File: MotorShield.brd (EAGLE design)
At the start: 85 x 56 mm, 119 parts, among them IC1 OPA4340E, IC2 OPA4340E, IC3 74HCT125D, X1 MSTBV2, X2 MSTBV8, X3 MSTBV8, X4 INPUTS, X5 BUTTON_LED, X6 DOTSTARS

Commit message: exchanged MCP3008 symbol and footprint https://github.com/hpbock/PCB-Designs/blob/master/!Libraries/MCP3008.lbr
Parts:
- removed U$58: MCP3008SO16, MSC3008:SO16
- added U$1: MCP3008SL, MCP3008:SO16
- C9: value 0,1uF -> 100nF; device eagle-ltspice:C0805 -> rcl:C0805
- moved X6 26.7 mm to (47.0, 29.8)
- moved X5 24.1 mm to (45.1, 44.5)
- moved C9 5.55 mm to (24.8, 41.9), flipped to the top
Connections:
- removed net 3,3V: C9.1, IC1.4, IC2.4, PCB1.1, PCB1.17, U$58.15, U$58.16
- new net +3,3V: IC1.4, IC2.4, PCB1.1, PCB1.17
- new net +3V3: C9.1, U$1.15, U$1.16
- net CH0: now also U$1.1; no longer U$58.1
- net CH1: now also U$1.2; no longer U$58.2
- net CH2: now also U$1.3; no longer U$58.3
- net CH3: now also U$1.4; no longer U$58.4
- net CH4: now also U$1.5; no longer U$58.5
- net CH5: now also U$1.6; no longer U$58.6
- net CH6: now also U$1.7; no longer U$58.7
- net CH7: now also U$1.8; no longer U$58.8
- net CLK: now also U$1.13; no longer U$58.13
- net CS_ADC: now also U$1.10; no longer U$58.10
- net DIN: now also U$1.11; no longer U$58.11
- net DOUT: now also U$1.12; no longer U$58.12
- net GND: now also U$1.14, U$1.9; no longer U$58.14, U$58.9
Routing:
- net +3V3: track 0.00 -> 6.10 mm, vias 0 -> 1

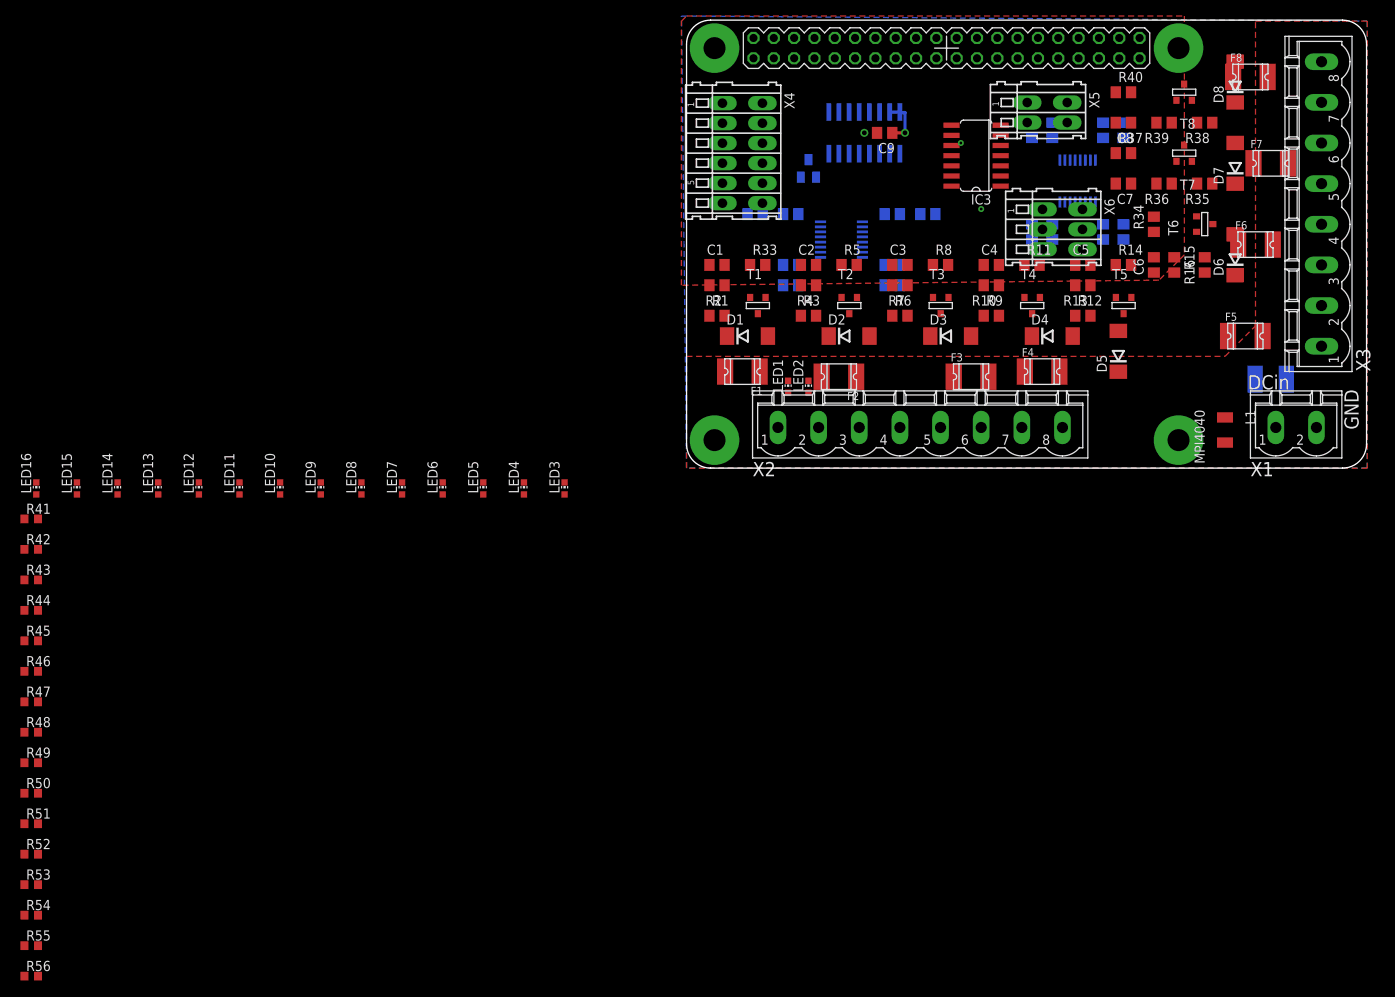
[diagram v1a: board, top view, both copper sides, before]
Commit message: added net classes and tried to place components for M1
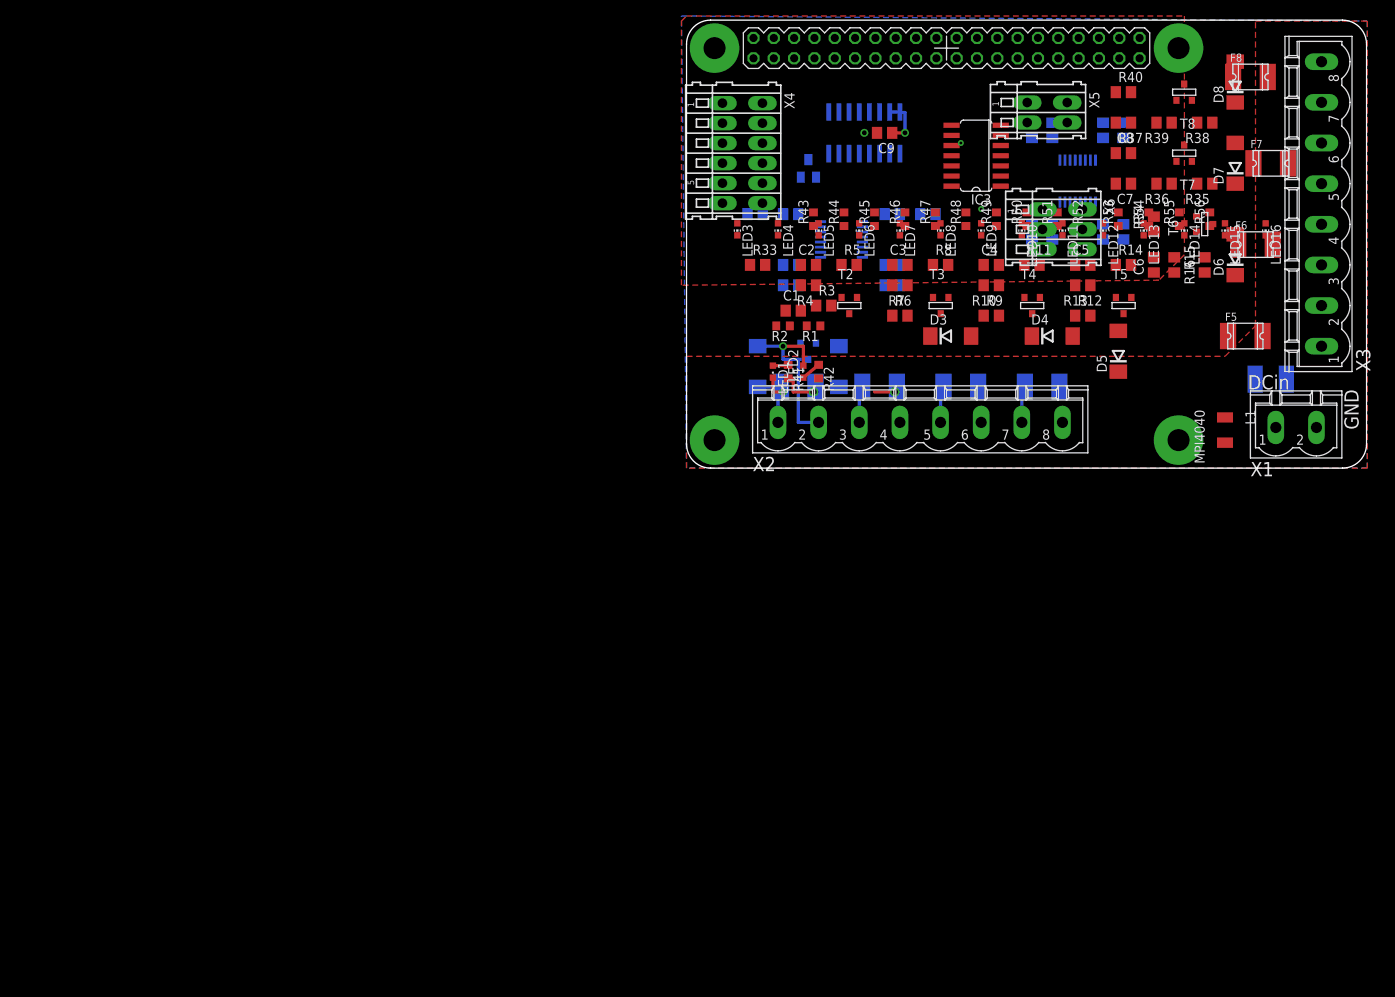
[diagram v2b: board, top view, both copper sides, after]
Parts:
- removed F1: 1812L, ptc-littlefuse:1812L
- added VIAMO: 1812L, ptc-littlefuse:1812L
- LED1, LED2: device led:CHIP-LED0603 -> led:CHIPLED_0603
- R1, R2: device rcl:R0805 -> rcl:R0603
- moved R56 175.1 mm to (65.4, 31.1), turned to 90 degrees
- moved R55 169.8 mm to (61.6, 31.1), turned to 90 degrees
- moved R54 164.6 mm to (57.8, 31.1), turned to 90 degrees
- moved R53 159.3 mm to (54.0, 31.1), turned to 90 degrees
- moved LED16 157.0 mm to (72.4, 29.8), turned to 180 degrees
- moved R52 154.1 mm to (50.2, 31.1), turned to 90 degrees
- moved R51 148.9 mm to (46.4, 31.1), turned to 90 degrees
- moved LED15 147.1 mm to (67.3, 29.8), turned to 180 degrees
- moved R50 143.7 mm to (42.5, 31.1), turned to 90 degrees
- moved R49 138.5 mm to (38.7, 31.1), turned to 90 degrees
- moved LED14 137.2 mm to (62.2, 29.8), turned to 180 degrees
- moved R48 133.3 mm to (34.9, 31.1), turned to 90 degrees
- moved R47 128.1 mm to (31.1, 31.1), turned to 90 degrees
- moved LED13 127.4 mm to (57.1, 29.8), turned to 180 degrees
- moved R46 123.0 mm to (27.3, 31.1), turned to 90 degrees
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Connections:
- removed net 5V: PCB1.2, PCB1.4
- net +24V: now also VIAMO.2; no longer F1.2
- net +3,3V: no longer PCB1.1
- net +3V3: now also PCB1.1
- net 24V/1A: now also VIAMO.1; no longer F1.1
- net VCC: now also PCB1.2, PCB1.4
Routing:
- net N$2: track 0.00 -> 23.4 mm, vias 0 -> 1
- net 24V/1A: track 0.00 -> 11.0 mm, vias 0 -> 1
- net +24V: track 0.00 -> 9.18 mm, vias 0 -> 2
- net N$9: track 0.00 -> 4.83 mm
- net N$12: track 0.00 -> 4.83 mm
- net N$13: track 0.00 -> 4.82 mm
- net N$30: track 0.00 -> 2.59 mm
- net N$28: track 0.00 -> 2.00 mm

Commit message: assigned values to protective resistors
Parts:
- R41, R42, R43, R44, R45, R46, R47, R48, R49, R50, R51, R52, R53, R54, R55, R56: value (none) -> 2k2
- renumbered VIAMO to F1
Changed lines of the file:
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@@
 <attribute name="OC_FARNELL" value="1283533" x="46.99" y="29.845" size="1.778" layer="27" rot="R270" display="off"/>
 </element>
-<element name="VIAMO" library="ptc-littlefuse" package="1812L" value="1812L" x="13.97" y="10.16" rot="MR180"/>
+<element name="F1" library="ptc-littlefuse" package="1812L" value="1812L" x="13.97" y="10.16" rot="MR180"/>
 <element name="F2" library="ptc-littlefuse" package="1812L" value="1812L" x="24.13" y="10.16" rot="MR180"/>
 <element name="F3" library="ptc-littlefuse" package="1812L" value="1812L" x="34.29" y="10.16" rot="MR180"/>
@@
 <element name="LED15" library="led" package="CHIP-LED0603" value="red" x="67.31" y="29.845" rot="R180"/>
 <element name="LED16" library="led" package="CHIP-LED0603" value="yellow" x="72.39" y="29.845" rot="R180"/>
-<element name="R41" library="rcl" package="R0603" value="" x="12.7" y="12.065" rot="R270"/>
-<element name="R42" library="rcl" package="R0603" value="" x="16.51" y="12.065" rot="R270"/>
-<element name="R43" library="rcl" package="R0603" value="" x="15.875" y="31.115" rot="R90"/>
-<element name="R44" library="rcl" package="R0603" value="" x="19.685" y="31.115" rot="R90"/>
-<element name="R45" library="rcl" package="R0603" value="" x="23.495" y="31.115" rot="R90"/>
-<element name="R46" library="rcl" package="R0603" value="" x="27.305" y="31.115" rot="R90"/>
-<element name="R47" library="rcl" package="R0603" value="" x="31.115" y="31.115" rot="R90"/>
-<element name="R48" library="rcl" package="R0603" value="" x="34.925" y="31.115" rot="R90"/>
-<element name="R49" library="rcl" package="R0603" value="" x="38.735" y="31.115" rot="R90"/>
-<element name="R50" library="rcl" package="R0603" value="" x="42.545" y="31.115" rot="R90"/>
-<element name="R51" library="rcl" package="R0603" value="" x="46.355" y="31.115" rot="R90"/>
-<element name="R52" library="rcl" package="R0603" value="" x="50.165" y="31.115" rot="R90"/>
-<element name="R53" library="rcl" package="R0603" value="" x="53.975" y="31.115" rot="R90"/>
-<element name="R54" library="rcl" package="R0603" value="" x="57.785" y="31.115" rot="R90"/>
-<element name="R55" library="rcl" package="R0603" value="" x="61.595" y="31.115" rot="R90"/>
-<element name="R56" library="rcl" package="R0603" value="" x="65.405" y="31.115" rot="R90"/>
+<element name="R41" library="rcl" package="R0603" value="2k2" x="12.7" y="12.065" rot="R270"/>
+<element name="R42" library="rcl" package="R0603" value="2k2" x="16.51" y="12.065" rot="R270"/>
+<element name="R43" library="rcl" package="R0603" value="2k2" x="15.875" y="31.115" rot="R90"/>
+<element name="R44" library="rcl" package="R0603" value="2k2" x="19.685" y="31.115" rot="R90"/>
+<element name="R45" library="rcl" package="R0603" value="2k2" x="23.495" y="31.115" rot="R90"/>
+<element name="R46" library="rcl" package="R0603" value="2k2" x="27.305" y="31.115" rot="R90"/>
+<element name="R47" library="rcl" package="R0603" value="2k2" x="31.115" y="31.115" rot="R90"/>
+<element name="R48" library="rcl" package="R0603" value="2k2" x="34.925" y="31.115" rot="R90"/>
+<element name="R49" library="rcl" package="R0603" value="2k2" x="38.735" y="31.115" rot="R90"/>
+<element name="R50" library="rcl" package="R0603" value="2k2" x="42.545" y="31.115" rot="R90"/>
+<element name="R51" library="rcl" package="R0603" value="2k2" x="46.355" y="31.115" rot="R90"/>
+<element name="R52" library="rcl" package="R0603" value="2k2" x="50.165" y="31.115" rot="R90"/>
+<element name="R53" library="rcl" package="R0603" value="2k2" x="53.975" y="31.115" rot="R90"/>
+<element name="R54" library="rcl" package="R0603" value="2k2" x="57.785" y="31.115" rot="R90"/>
+<element name="R55" library="rcl" package="R0603" value="2k2" x="61.595" y="31.115" rot="R90"/>
+<element name="R56" library="rcl" package="R0603" value="2k2" x="65.405" y="31.115" rot="R90"/>
 <element name="U$1" library="MCP3008" package="SO16" value="MCP3008SL" x="22.225" y="41.91" rot="MR0"/>
 <element name="C9" library="rcl" package="C0805" value="100nF" x="24.765" y="41.91" rot="R180"/>
@@
 <contactref element="D1" pad="C"/>
 <contactref element="X2" pad="1"/>
-<contactref element="VIAMO" pad="1"/>
+<contactref element="F1" pad="1"/>
 <contactref element="LED1" pad="C"/>
 <wire x1="11.81" y1="10.16" x2="11.43" y2="10.16" width="0.4064" layer="16"/>
@@
 <contactref element="F3" pad="2"/>
 <contactref element="F2" pad="2"/>
-<contactref element="VIAMO" pad="2"/>
+<contactref element="F1" pad="2"/>
 <polygon width="0.762" layer="1" isolate="0.762">
 <vertex x="0" y="13.97"/>

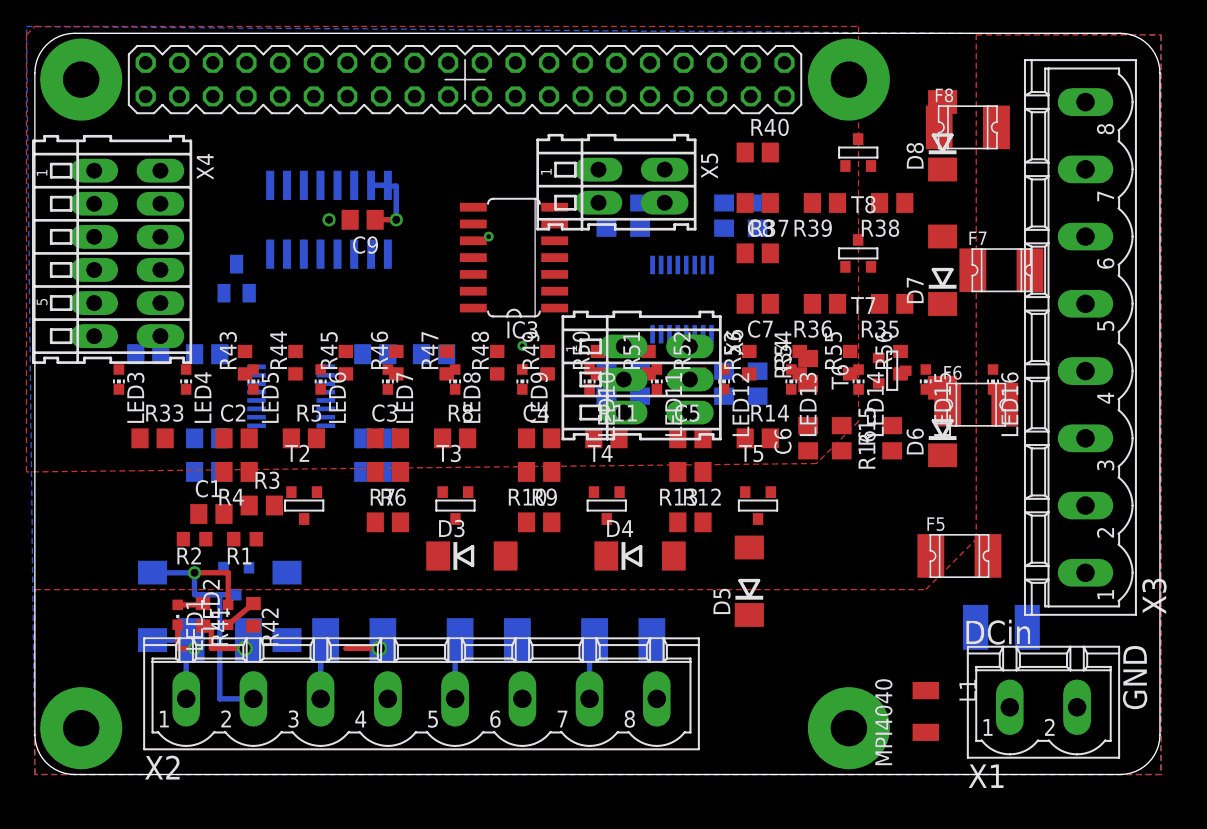
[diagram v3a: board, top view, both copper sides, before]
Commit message: routed devices for M4 and M3
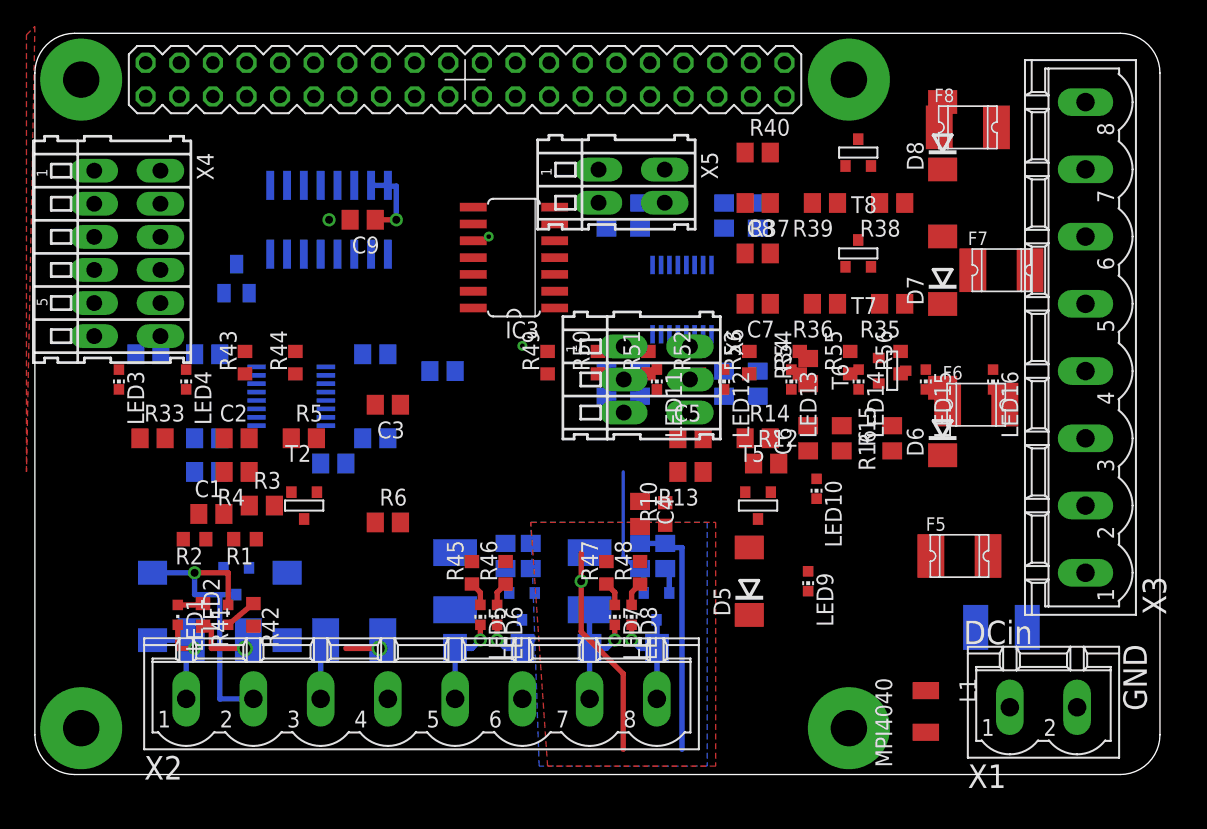
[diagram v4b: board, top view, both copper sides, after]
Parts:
- R10: device rcl:R0805 -> rcl:R0603
- moved LED9 26.4 mm to (58.4, 14.6)
- moved LED5 24.7 mm to (33.7, 12.1)
- moved LED7 24.7 mm to (43.8, 12.1)
- moved LED8 22.2 mm to (45.1, 12.1)
- moved LED6 22.2 mm to (34.9, 12.1)
- moved R47 19.9 mm to (43.2, 15.2)
- moved R48 19.2 mm to (45.7, 15.2)
- moved LED10 19.0 mm to (59.1, 21.6)
- moved R45 18.5 mm to (33.0, 15.2)
- moved R46 17.9 mm to (35.6, 15.2)
- moved R7 12.5 mm to (37.5, 16.5), flipped to the bottom, turned to 90 degrees
- moved R10 10.0 mm to (47.6, 19.7), turned to 90 degrees
- moved R9 9.86 mm to (47.6, 16.5), flipped to the bottom, turned to 270 degrees
- moved R8 9.67 mm to (35.6, 16.5), flipped to the bottom, turned to 270 degrees
- moved C4 9.52 mm to (45.7, 19.7), turned to 270 degrees
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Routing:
- net GND: track 0.00 -> 18.7 mm
- net +24V: track 9.18 -> 26.0 mm, vias 2 -> 3
- net M4: track 0.00 -> 9.97 mm
- net N$26: track 0.00 -> 9.35 mm, vias 0 -> 1
- net N$9: track 4.83 -> 10.1 mm, vias 0 -> 1
- net N$17: track 0.00 -> 3.33 mm, vias 0 -> 1
- net N$12: track 4.83 -> 7.15 mm, vias 0 -> 1
- net N$29: track 0.00 -> 1.97 mm
- net N$41: track 0.00 -> 1.84 mm
- net N$44: track 0.00 -> 1.84 mm
- net N$43: track 0.00 -> 1.84 mm
- net N$42: track 0.00 -> 1.84 mm
